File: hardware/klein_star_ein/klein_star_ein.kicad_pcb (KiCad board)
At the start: 6 copper layers, 100 x 90 mm, 184 parts, among them J1 USB_A, J10 AudioJack3_Ground_Switch, J11 AudioJack3_Ground_Switch, J12 AudioJack3_Ground_Switch, J2 DB15_Female_HighDensity_Mount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, J3 Bus_PCI_Express_x1, J4 1367073-1, J5 RJ45_LED_Shielded, J6 USB_C_Receptacle, J7 MEM2051-00-195-00-A, J8 AudioJack3_Ground_Switch, J9 AudioJack3_Ground_Switch, U1 ECP5UM25, U10 SN74ALVC245PWR, U11 KSZ9021RL, U12 TUSB2036, U13 TPS2041B, U2 MT41K512M16, U3 MT41K512M16, U4 FT2232HQ, U5 W25Q128JVS, U6 USB3300-EZK, U7 USB3300-EZK, U8 SN74ALVC245PWR, U9 SN74ALVC245PWR

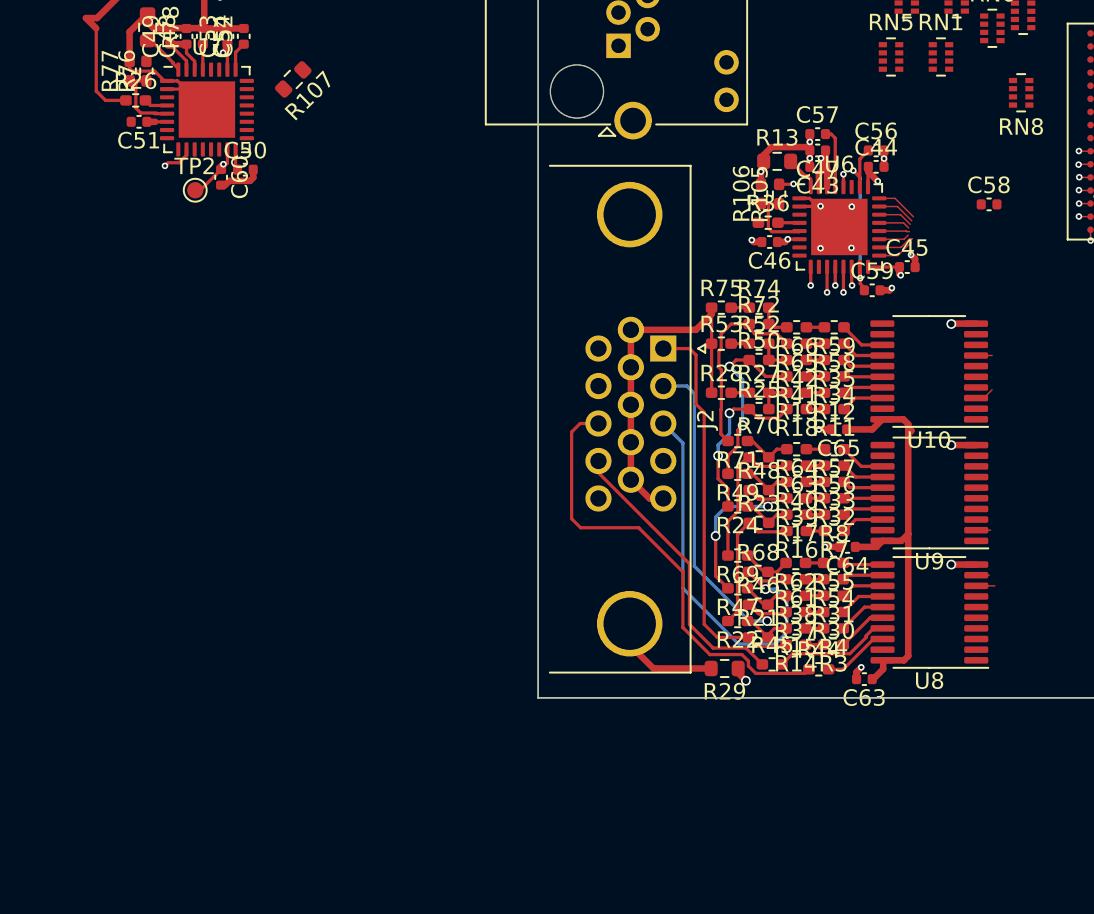
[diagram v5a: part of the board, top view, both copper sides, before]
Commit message: changed VGA drivers to use resistor networks
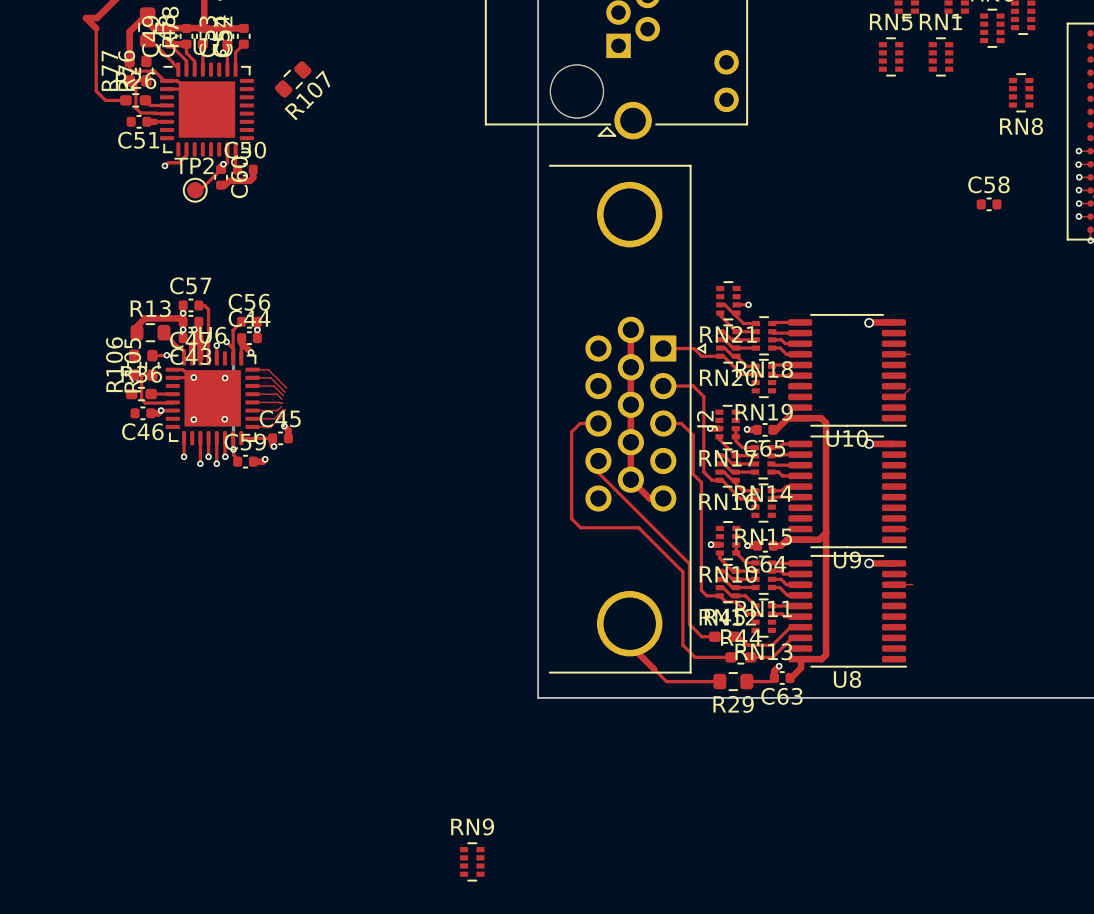
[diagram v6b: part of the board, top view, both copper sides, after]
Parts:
- removed R11, R12, R14, R15, R16, R17, R18, R19, R21, R22, R23, R24, R25, R27, R28, R3, R30, R31, R32, R33, R34, R35, R37, R38, R39, R4, R40, R41, R42, R46, R47, R48, R49, R50, R52, R53, R54, R55, R56, R57, R58, R59, R61, R62, R63, R64, R65, R66, R68, R69, R7, R70, R71, R72, R74, R75, R8: R, Resistor_SMD:R_0402_1005Metric_Pad0.72x0.64mm_HandSolder
- added RN10: 51R, Resistor_SMD:R_Array_Concave_4x0402, F.Cu at (109.6, 140.4)
- added RN11: 51R, Resistor_SMD:R_Array_Concave_4x0402, F.Cu at (111.8, 142.5)
- added RN12: 51R, Resistor_SMD:R_Array_Concave_4x0402, F.Cu at (109.6, 143.0)
- added RN13: 51R, Resistor_SMD:R_Array_Concave_4x0402, F.Cu at (111.8, 145.1)
- added RN14: 51R, Resistor_SMD:R_Array_Concave_4x0402, F.Cu at (111.8, 135.4)
- added RN15: 51R, Resistor_SMD:R_Array_Concave_4x0402, F.Cu at (111.8, 138.1)
- added RN16: 51R, Resistor_SMD:R_Array_Concave_4x0402, F.Cu at (109.6, 135.9)
- added RN17: 51R, Resistor_SMD:R_Array_Concave_4x0402, F.Cu at (109.6, 133.3)
- added RN18: 51R, Resistor_SMD:R_Array_Concave_4x0402, F.Cu at (111.8, 127.9)
- added RN19: 51R, Resistor_SMD:R_Array_Concave_4x0402, F.Cu at (111.8, 130.5)
- added RN20: 51R, Resistor_SMD:R_Array_Concave_4x0402, F.Cu at (109.6, 128.4)
- added RN21: 51R, Resistor_SMD:R_Array_Concave_4x0402, F.Cu at (109.6, 125.7)
- added RN9: 51R, Resistor_SMD:R_Array_Concave_4x0402, F.Cu at (94.0, 160.0)
- moved C46 39.7 mm to (73.9, 132.6)
- moved C47 39.7 mm to (76.8, 127.0)
- moved C56 39.7 mm to (80.4, 127.0)
- moved C57 39.7 mm to (76.8, 126.0)
- moved C59 39.7 mm to (80.1, 135.6)
- moved R105 39.7 mm to (74.4, 129.7)
- moved R106 39.7 mm to (73.3, 129.7)
- moved R13 39.7 mm to (74.3, 127.7)
- moved R36 39.7 mm to (73.8, 131.4)
- moved U6 39.7 mm to (78.1, 131.7)
- moved C43 39.7 mm to (76.8, 128.0)
- moved C44 39.7 mm to (80.4, 128.0)
- moved C45 39.7 mm to (82.3, 134.1)
- moved U10 5.02 mm to (116.9, 130.0)
- moved C64 5.02 mm to (111.9, 140.7)
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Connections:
- U10 pad 11: unconnected-(U10-Pad11) -> /VGA_BUF_B_5
- U10 pad 12: unconnected-(U10-Pad12) -> /VGA_BUF_B_4
- U10 pad 13: /VGA_BUF_B_5 -> /VGA_BUF_B_3
- U10 pad 14: /VGA_BUF_B_4 -> /VGA_BUF_B_2
- U10 pad 15: /VGA_BUF_G_5 -> /VGA_BUF_B_1
- U10 pad 16: /VGA_BUF_G_4 -> /VGA_BUF_B_0
- U10 pad 17: /VGA_BUF_R_5 -> unconnected-(U10-Pad17)
- U10 pad 18: /VGA_BUF_R_4 -> unconnected-(U10-Pad18)
- U8 pad 11: /VGA_BUF_B_1 -> /VGA_BUF_R_5
- U8 pad 12: /VGA_BUF_B_0 -> /VGA_BUF_R_4
- U8 pad 13: /VGA_BUF_G_1 -> /VGA_BUF_R_3
- U8 pad 14: /VGA_BUF_G_0 -> /VGA_BUF_R_2
- U9 pad 11: unconnected-(U9-Pad11) -> /VGA_BUF_G_5
- U9 pad 12: unconnected-(U9-Pad12) -> /VGA_BUF_G_4
- U9 pad 13: /VGA_BUF_B_3 -> /VGA_BUF_G_3
- U9 pad 14: /VGA_BUF_B_2 -> /VGA_BUF_G_2
- U9 pad 15: /VGA_BUF_G_3 -> /VGA_BUF_G_1
- U9 pad 16: /VGA_BUF_G_2 -> /VGA_BUF_G_0
- U9 pad 17: /VGA_BUF_R_3 -> unconnected-(U9-Pad17)
- U9 pad 18: /VGA_BUF_R_2 -> unconnected-(U9-Pad18)
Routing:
- net /VGA_AR: track 24.4 -> 6.30 mm
- net Net-(R65-Pad2): track 12.0 -> 0.00 mm
- net /VGA_AG: track 22.7 -> 11.2 mm, vias 1 -> 0
- net Net-(R41-Pad2): track 11.3 -> 0.00 mm, vias 2 -> 0
- net Net-(R39-Pad2): track 11.3 -> 0.00 mm, vias 2 -> 0
- net GND: track 135.2 -> 124.1 mm
- net Net-(R18-Pad2): track 10.3 -> 0.00 mm, vias 2 -> 0
- net /VGA_AB: track 25.4 -> 15.7 mm, vias 1 -> 0
- net Net-(R63-Pad2): track 9.15 -> 0.00 mm
- net Net-(R16-Pad2): track 9.09 -> 0.00 mm
- net Net-(J2-Pad13): track 27.8 -> 23.0 mm
- net Net-(J2-Pad14): track 17.8 -> 14.2 mm
- net Net-(R17-Pad2): track 3.03 -> 0.00 mm
- net Net-(R64-Pad2): track 3.03 -> 0.00 mm
- net Net-(R40-Pad2): track 3.03 -> 0.00 mm
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
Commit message: a
a
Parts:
- J5: value RJ45_LED_Shielded -> ARJM11C7-502-AB-ER2-T; footprint Connector_RJ:RJ45_Amphenol_RJHSE538X -> footprints:ABRACON_ARJM11C7-502-AB-ER2-T
- moved RN1 66.2 mm to (59.3, 130.2)
- moved RN2 66.2 mm to (57.2, 126.6)
- moved RN6 66.2 mm to (62.5, 128.4)
- moved RN4 66.2 mm to (60.3, 126.6)
- moved RN7 66.2 mm to (64.3, 127.7)
- moved RN8 66.2 mm to (64.2, 132.4)
- moved U5 66.2 mm to (58.0, 119.1)
- moved RN5 66.2 mm to (56.3, 130.2)
- moved C62 59.7 mm to (132.0, 87.6), turned to 0 degrees
- moved R77 58.8 mm to (125.8, 85.7), turned to 0 degrees
- moved R78 58.7 mm to (128.4, 86.8), turned to 180 degrees
- moved C61 58.1 mm to (135.4, 91.0), turned to -90 degrees
- moved R26 57.5 mm to (124.0, 86.1), turned to -90 degrees
- moved R76 57.4 mm to (125.8, 86.7), turned to 0 degrees
- moved C51 56.7 mm to (122.7, 86.3), turned to 90 degrees
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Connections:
- J5 pad 1: unconnected-(J5-Pad1) -> Net-(U11-Pad1)
- J5 pad 10: unconnected-(J5-Pad10) -> Net-(U11-Pad15)
- J5 pad 2: unconnected-(J5-Pad2) -> Net-(U11-Pad2)
- J5 pad 3: unconnected-(J5-Pad3) -> Net-(U11-Pad7)
- J5 pad 4: unconnected-(J5-Pad4) -> Net-(U11-Pad8)
- J5 pad 7: unconnected-(J5-Pad7) -> Net-(U11-Pad10)
- J5 pad 8: unconnected-(J5-Pad8) -> Net-(U11-Pad11)
- J5 pad 9: unconnected-(J5-Pad9) -> Net-(U11-Pad14)
- U11 pad 1: unconnected-(U11-Pad1) -> Net-(U11-Pad1)
- U11 pad 10: unconnected-(U11-Pad10) -> Net-(U11-Pad10)
- U11 pad 11: unconnected-(U11-Pad11) -> Net-(U11-Pad11)
- U11 pad 14: unconnected-(U11-Pad14) -> Net-(U11-Pad14)
- U11 pad 15: unconnected-(U11-Pad15) -> Net-(U11-Pad15)
- U11 pad 2: unconnected-(U11-Pad2) -> Net-(U11-Pad2)
- U11 pad 7: unconnected-(U11-Pad7) -> Net-(U11-Pad7)
- U11 pad 8: unconnected-(U11-Pad8) -> Net-(U11-Pad8)
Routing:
- net GND: track 124.1 -> 102.1 mm, vias 41 -> 21
- net /DRAM_DATA_20: track 21.4 -> 0.00 mm, vias 2 -> 0
- net /DRAM_DATA_8: track 19.9 -> 0.00 mm, vias 2 -> 0
- net /DRAM_DATA_10: track 19.8 -> 0.00 mm, vias 2 -> 0
- net /DRAM_DM2: track 19.8 -> 0.00 mm, vias 2 -> 0
- net /DRAM_DATA_5: track 19.8 -> 0.00 mm, vias 2 -> 0
- net /DRAM_DQS2_P: track 19.8 -> 0.00 mm, vias 2 -> 0
- net /DRAM_DATA_14: track 19.8 -> 0.00 mm, vias 2 -> 0
- net /DRAM_DQS2_N: track 19.8 -> 0.00 mm, vias 2 -> 0
- net /DRAM_DQS1_N: track 19.8 -> 0.00 mm, vias 2 -> 0
- net /DRAM_DM3: track 19.8 -> 0.00 mm, vias 2 -> 0
- net /DRAM_DQS0_N: track 19.8 -> 0.00 mm, vias 2 -> 0
- net /DRAM_DQS1_P: track 19.8 -> 0.00 mm, vias 2 -> 0
- net /DRAM_DATA_29: track 19.8 -> 0.00 mm, vias 2 -> 0
- net /DRAM_DATA_27: track 19.8 -> 0.00 mm, vias 2 -> 0
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
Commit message: dram layout
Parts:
- removed R1, R6: 0R, Resistor_SMD:R_0603_1608Metric
- removed RN8: 51R, Resistor_SMD:R_Array_Concave_4x0402
- added C66: 470n, Capacitor_SMD:C_0402_1005Metric, F.Cu at (170.2, 124.7)
- C11, C13, C39, C40, C41, C42, C55, C8, R79, R80: moved to B.Cu
- moved C2 116.4 mm to (158.9, 121.2), turned to 180 degrees
- moved C7 113.8 mm to (159.2, 130.1), turned to 90 degrees
- moved C36 111.0 mm to (161.9, 132.9), turned to 180 degrees
- moved RN5 110.1 mm to (164.8, 148.8), turned to 90 degrees
- moved RN6 109.7 mm to (170.7, 146.4)
- moved RN7 107.6 mm to (170.7, 143.7)
- moved RN2 103.1 mm to (158.8, 144.2)
- moved C3 102.2 mm to (170.6, 129.2), turned to 90 degrees
- moved RN4 100.6 mm to (158.8, 146.8)
- moved RN1 100.1 mm to (158.8, 141.6)
- moved C8 98.5 mm to (160.2, 146.3), turned to -90 degrees
- moved C9 93.8 mm to (159.2, 125.1), turned to 90 degrees
- moved C37 90.8 mm to (167.5, 133.3)
- moved C35 90.1 mm to (159.2, 136.8), turned to -90 degrees
- moved C17 90.1 mm to (159.2, 134.7), turned to -90 degrees
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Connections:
- C1 pad 1: /DRAM_1_VCORE -> 1V35_DRAM_VCORE
- C10 pad 1: /DRAM_2_VCORE -> 1V35_DRAM_VCORE
- C12 pad 1: /DRAM_1_VCORE -> 1V35_DRAM_VCORE
- C13 pad 1: /DRAM_2_VCORE -> 1V35_DRAM_VCORE
- C14 pad 1: /DRAM_2_VCORE -> 1V35_DRAM_VCORE
- C15 pad 1: /DRAM_1_VCORE -> 1V35_DRAM_VCORE
- C16 pad 1: /DRAM_2_VCORE -> 1V35_DRAM_VCORE
- C17 pad 1: /DRAM_2_VCORE -> 1V35_DRAM_VCORE
- C18 pad 1: /DRAM_1_VCORE -> 1V35_DRAM_VCORE
- C19 pad 1: /DRAM_2_VCORE -> 1V35_DRAM_VCORE
- C2 pad 1: /DRAM_1_VCORE -> 1V35_DRAM_VCORE
- C20 pad 1: /DRAM_1_VCORE -> 1V35_DRAM_VCORE
- C3 pad 1: /DRAM_1_VCORE -> 1V35_DRAM_VCORE
- C35 pad 1: /DRAM_2_VCORE -> 1V35_DRAM_VCORE
- C36 pad 1: /DRAM_1_VCORE -> 1V35_DRAM_VCORE
- C37 pad 1: /DRAM_2_VCORE -> 1V35_DRAM_VCORE
- C38 pad 1: /DRAM_1_VCORE -> 1V35_DRAM_VCORE
- C39 pad 1: /DRAM_2_VCORE -> 1V35_DRAM_VCORE
- C4 pad 1: /DRAM_2_VCORE -> 1V35_DRAM_VCORE
- C5 pad 1: /DRAM_1_VCORE -> 1V35_DRAM_VCORE
- C6 pad 1: /DRAM_2_VCORE -> 1V35_DRAM_VCORE
- C7 pad 1: /DRAM_1_VCORE -> 1V35_DRAM_VCORE
- C8 pad 1: /DRAM_2_VCORE -> 1V35_DRAM_VCORE
- C9 pad 1: /DRAM_1_VCORE -> 1V35_DRAM_VCORE
- RN1 pad 1: /DRAM_ADDR_13 -> GND
- RN1 pad 2: /DRAM_ADDR_7 -> GND
- RN1 pad 3: /DRAM_ADDR_9 -> GND
- RN1 pad 4: /DRAM_ADDR_5 -> GND
- RN1 pad 5: GND -> /DRAM_nCS
- RN1 pad 6: GND -> /DRAM_ODT
- RN1 pad 7: GND -> /DRAM_nCAS
- RN1 pad 8: GND -> /DRAM_nRAS
- RN2 pad 1: /DRAM_ADDR_2 -> GND
- RN2 pad 2: /DRAM_ADDR_3 -> GND
- RN2 pad 3: /DRAM_ADDR_0 -> GND
- RN2 pad 4: /DRAM_ADDR_BA2 -> GND
- RN2 pad 5: GND -> /DRAM_ADDR_3
- RN2 pad 6: GND -> /DRAM_ADDR_0
- RN2 pad 7: GND -> /DRAM_ADDR_BA2
- RN2 pad 8: GND -> /DRAM_ADDR_BA0
- RN4 pad 1: /DRAM_ADDR_BA0 -> GND
- RN4 pad 2: /DRAM_nCS -> GND
- RN4 pad 3: /DRAM_nWE -> GND
- RN4 pad 4: /DRAM_ODT -> unconnected-(RN4-Pad4)
- RN4 pad 5: GND -> unconnected-(RN4-Pad5)
- RN4 pad 6: GND -> /DRAM_ADDR_7
- RN4 pad 7: GND -> /DRAM_ADDR_2
- RN4 pad 8: GND -> /DRAM_ADDR_5
- RN5 pad 1: /DRAM_nCAS -> GND
- RN5 pad 2: /DRAM_nRAS -> GND
- RN5 pad 3: unconnected-(RN5-Pad3) -> GND
- RN5 pad 4: unconnected-(RN5-Pad4) -> GND
- RN5 pad 5: unconnected-(RN5-Pad5) -> /DRAM_ADDR_14
- RN5 pad 6: unconnected-(RN5-Pad6) -> /DRAM_ADDR_11
- RN5 pad 7: GND -> /DRAM_ADDR_9
- RN5 pad 8: GND -> /DRAM_ADDR_13
- RN6 pad 1: /DRAM_ADDR_11 -> /DRAM_ADDR_BA1
- RN6 pad 2: /DRAM_ADDR_6 -> /DRAM_ADDR_4
- RN6 pad 3: /DRAM_ADDR_8 -> /DRAM_ADDR_6
- RN6 pad 4: /DRAM_ADDR_14 -> /DRAM_ADDR_8
- RN7 pad 1: /DRAM_ADDR_BA1 -> /DRAM_ADDR_10
- RN7 pad 2: /DRAM_ADDR_12 -> /DRAM_ADDR_15
- RN7 pad 3: /DRAM_ADDR_1 -> /DRAM_ADDR_12
- RN7 pad 4: /DRAM_ADDR_4 -> /DRAM_ADDR_1
- U1 pad A12: Net-(U1-PadA13) -> /DRAM_nWE
- U1 pad A13: Net-(U1-PadA13) -> /DRAM_ADDR_BA1
- U1 pad A14: Net-(U1-PadA13) -> /DRAM_ADDR_4
- U1 pad A16: Net-(U1-PadA13) -> /DRAM_ADDR_14
- U1 pad A17: Net-(U1-PadA13) -> /DRAM_nRAS
- U1 pad A18: Net-(U1-PadA13) -> /DRAM_ADDR_BA0
- U1 pad A19: Net-(U1-PadA13) -> /DRAM_nCAS
- U1 pad B12: Net-(U1-PadA13) -> /DRAM_ADDR_15
- U1 pad B13: Net-(U1-PadA13) -> /DRAM_ADDR_1
- U1 pad B15: Net-(U1-PadA13) -> /DRAM_ADDR_6
- U1 pad B16: Net-(U1-PadA13) -> unconnected-(U1-PadB16)
- U1 pad B17: Net-(U1-PadA13) -> unconnected-(U1-PadB17)
- U1 pad B18: Net-(U1-PadA13) -> unconnected-(U1-PadB18)
- U1 pad B19: Net-(U1-PadA13) -> /DRAM_nCS
- U1 pad B20: Net-(U1-PadA13) -> /DRAM_ADDR_12
- U1 pad B3: /DRAM_DATA_6 -> unconnected-(U1-PadB3)
- U1 pad B4: /DRAM_DATA_4 -> unconnected-(U1-PadB4)
- U1 pad C12: Net-(U1-PadA13) -> /DRAM_ADDR_10
- U1 pad C13: Net-(U1-PadA13) -> unconnected-(U1-PadC13)
- U1 pad C14: Net-(U1-PadA13) -> /DRAM_ADDR_11
- U1 pad C15: Net-(U1-PadA13) -> /DRAM_ADDR_5
- U1 pad C16: Net-(U1-PadA13) -> /DRAM_ADDR_8
- U1 pad C17: Net-(U1-PadA13) -> /DRAM_ADDR_0
- U1 pad C18: /DRAM_DM2 -> /DRAM_DATA_4
- U1 pad C4: /DRAM_DATA_5 -> unconnected-(U1-PadC4)
- U1 pad C5: /DRAM_DATA_7 -> unconnected-(U1-PadC5)
- U1 pad D11: Net-(U1-PadA13) -> /DRAM_CKE
- U1 pad D12: Net-(U1-PadA13) -> /DRAM_CLK_P
- U1 pad D13: Net-(U1-PadA13) -> /DRAM_ADDR_3
- U1 pad D14: Net-(U1-PadA13) -> /DRAM_nRESET
- U1 pad D15: Net-(U1-PadA13) -> /DRAM_ADDR_2
- U1 pad D16: Net-(U1-PadA13) -> /DRAM_ADDR_BA2
- U1 pad D17: /DRAM_DATA_19 -> /DRAM_DATA_6
- U1 pad D18: /DRAM_DATA_17 -> /DRAM_DATA_7
- U1 pad D19: /DRAM_DATA_30 -> unconnected-(U1-PadD19)
- U1 pad D20: unconnected-(U1-PadD20) -> DRAM_VREF
- U1 pad D5: /DRAM_DQS0_N -> unconnected-(U1-PadD5)
- U1 pad E1: /DRAM_DATA_11 -> unconnected-(U1-PadE1)
- U1 pad E11: Net-(U1-PadA13) -> unconnected-(U1-PadE11)
- U1 pad E12: Net-(U1-PadA13) -> /DRAM_CLK_N
- U1 pad E13: Net-(U1-PadA13) -> /DRAM_ADDR_13
- U1 pad E14: Net-(U1-PadA13) -> /DRAM_ADDR_7
- U1 pad E15: Net-(U1-PadA13) -> /DRAM_ADDR_9
- U1 pad E16: /DRAM_DATA_21 -> unconnected-(U1-PadE16)
- U1 pad E17: /DRAM_DATA_22 -> unconnected-(U1-PadE17)
- U1 pad E18: /DRAM_DATA_23 -> /DRAM_DATA_5
- U1 pad E19: /DRAM_DATA_28 -> /DRAM_DM1
- U1 pad E2: /DRAM_DATA_13 -> unconnected-(U1-PadE2)
- U1 pad E4: /DRAM_DQS0_P -> unconnected-(U1-PadE4)
- U1 pad F11: unconnected-(U1-PadF11) -> 1V35_DRAM_VCORE
- U1 pad F12: unconnected-(U1-PadF12) -> 1V35_DRAM_VCORE
- U1 pad F16: /DRAM_DATA_18 -> unconnected-(U1-PadF16)
- U1 pad F17: /DRAM_DQS2_P -> /DRAM_DQS0_P
- U1 pad F18: /DRAM_DATA_16 -> unconnected-(U1-PadF18)
- U1 pad F19: /DRAM_DATA_26 -> /DRAM_DATA_8
- U1 pad F2: /DRAM_DATA_15 -> unconnected-(U1-PadF2)
- U1 pad F20: unconnected-(U1-PadF20) -> /DRAM_DATA_10
- U1 pad F3: /DRAM_DATA_14 -> unconnected-(U1-PadF3)
- U1 pad G16: /DRAM_DATA_20 -> /DRAM_DATA_1
- U1 pad G18: /DRAM_DQS2_N -> /DRAM_DQS0_N
- U1 pad G19: /DRAM_DQS3_P -> /DRAM_DQS1_P
- U1 pad G20: /DRAM_DATA_24 -> unconnected-(U1-PadG20)
- U1 pad G3: /DRAM_DATA_12 -> unconnected-(U1-PadG3)
- U1 pad G5: /DRAM_DQS1_N -> unconnected-(U1-PadG5)
- U1 pad H14: +1V35 -> 1V35_DRAM_VCORE
- U1 pad H15: +1V35 -> 1V35_DRAM_VCORE
- U1 pad H16: unconnected-(U1-PadH16) -> /DRAM_DATA_3
- U1 pad H17: unconnected-(U1-PadH17) -> /DRAM_DM0
- U1 pad H20: /DRAM_DQS3_N -> /DRAM_DQS1_N
- U1 pad H3: /DRAM_DATA_8 -> unconnected-(U1-PadH3)
- U1 pad H4: /DRAM_DQS1_P -> unconnected-(U1-PadH4)
- U1 pad H5: /DRAM_DATA_10 -> unconnected-(U1-PadH5)
- U1 pad J15: +1V35 -> 1V35_DRAM_VCORE
- U1 pad J16: unconnected-(U1-PadJ16) -> /DRAM_DATA_0
- U1 pad J17: unconnected-(U1-PadJ17) -> /DRAM_DATA_2
- U1 pad J18: /DRAM_DM3 -> /DRAM_DATA_13
- U1 pad J19: /DRAM_DATA_31 -> /DRAM_DATA_9
- U1 pad J20: /DRAM_DATA_25 -> /DRAM_DATA_11
- U1 pad K18: unconnected-(U1-PadK18) -> /DRAM_DATA_15
- U1 pad K19: /DRAM_DATA_29 -> /DRAM_DATA_12
- U1 pad K20: /DRAM_DATA_27 -> /DRAM_DATA_14
- U1 pad L14: unconnected-(U1-PadL14) -> 1V35_DRAM_VCORE
- U1 pad L15: unconnected-(U1-PadL15) -> 1V35_DRAM_VCORE
- U1 pad L17: unconnected-(U1-PadL17) -> /DRAM_DATA_25
- U1 pad L18: unconnected-(U1-PadL18) -> /DRAM_DATA_26
- U1 pad M15: unconnected-(U1-PadM15) -> 1V35_DRAM_VCORE
- U1 pad M17: unconnected-(U1-PadM17) -> /DRAM_DQS3_N
- U1 pad M18: unconnected-(U1-PadM18) -> /DRAM_DATA_30
- U1 pad M19: unconnected-(U1-PadM19) -> /DRAM_DATA_29
- U1 pad M20: unconnected-(U1-PadM20) -> /DRAM_DATA_28
- U1 pad N16: unconnected-(U1-PadN16) -> /DRAM_DQS3_P
- U1 pad N18: unconnected-(U1-PadN18) -> /DRAM_DATA_31
- U1 pad P16: unconnected-(U1-PadP16) -> DRAM_VREF
- U1 pad P17: unconnected-(U1-PadP17) -> /DRAM_DATA_27
- U1 pad P19: unconnected-(U1-PadP19) -> /DRAM_DATA_16
- U1 pad P20: unconnected-(U1-PadP20) -> /DRAM_DATA_23
- U1 pad R16: unconnected-(U1-PadR16) -> /DRAM_DATA_24
- U1 pad R17: unconnected-(U1-PadR17) -> /DRAM_DM3
- U1 pad R18: unconnected-(U1-PadR18) -> /DRAM_DQS2_N
- U1 pad T17: unconnected-(U1-PadT17) -> /DRAM_DM2
- U1 pad T19: unconnected-(U1-PadT19) -> /DRAM_DQS2_P
- U1 pad T20: unconnected-(U1-PadT20) -> /DRAM_DATA_20
- U1 pad U16: unconnected-(U1-PadU16) -> /DRAM_DATA_21
- U1 pad U17: unconnected-(U1-PadU17) -> /DRAM_DATA_19
- U1 pad U18: unconnected-(U1-PadU18) -> /DRAM_DATA_17
- U1 pad U19: unconnected-(U1-PadU19) -> /DRAM_DATA_22
- U1 pad U20: unconnected-(U1-PadU20) -> /DRAM_DATA_18
- U2 pad A1: /DRAM_1_VCORE -> 1V35_DRAM_VCORE
- U2 pad A8: /DRAM_1_VCORE -> 1V35_DRAM_VCORE
- U2 pad B2: /DRAM_1_VCORE -> 1V35_DRAM_VCORE
- U2 pad C1: /DRAM_1_VCORE -> 1V35_DRAM_VCORE
- U2 pad C9: /DRAM_1_VCORE -> 1V35_DRAM_VCORE
- U2 pad D2: /DRAM_1_VCORE -> 1V35_DRAM_VCORE
- U2 pad D9: /DRAM_1_VCORE -> 1V35_DRAM_VCORE
- U2 pad E9: /DRAM_1_VCORE -> 1V35_DRAM_VCORE
- U2 pad F1: /DRAM_1_VCORE -> 1V35_DRAM_VCORE
- U2 pad G7: /DRAM_1_VCORE -> 1V35_DRAM_VCORE
- U2 pad H2: /DRAM_1_VCORE -> 1V35_DRAM_VCORE
- U2 pad H9: /DRAM_1_VCORE -> 1V35_DRAM_VCORE
- U2 pad K2: /DRAM_1_VCORE -> 1V35_DRAM_VCORE
- U2 pad K8: /DRAM_1_VCORE -> 1V35_DRAM_VCORE
- U2 pad N1: /DRAM_1_VCORE -> 1V35_DRAM_VCORE
- U2 pad N9: /DRAM_1_VCORE -> 1V35_DRAM_VCORE
- U2 pad R1: /DRAM_1_VCORE -> 1V35_DRAM_VCORE
- U2 pad R9: /DRAM_1_VCORE -> 1V35_DRAM_VCORE
- U3 pad A1: /DRAM_2_VCORE -> 1V35_DRAM_VCORE
- U3 pad A8: /DRAM_2_VCORE -> 1V35_DRAM_VCORE
- U3 pad B2: /DRAM_2_VCORE -> 1V35_DRAM_VCORE
- U3 pad C1: /DRAM_2_VCORE -> 1V35_DRAM_VCORE
- U3 pad C9: /DRAM_2_VCORE -> 1V35_DRAM_VCORE
- U3 pad D2: /DRAM_2_VCORE -> 1V35_DRAM_VCORE
- U3 pad D9: /DRAM_2_VCORE -> 1V35_DRAM_VCORE
- U3 pad E9: /DRAM_2_VCORE -> 1V35_DRAM_VCORE
- U3 pad F1: /DRAM_2_VCORE -> 1V35_DRAM_VCORE
- U3 pad G7: /DRAM_2_VCORE -> 1V35_DRAM_VCORE
- U3 pad H2: /DRAM_2_VCORE -> 1V35_DRAM_VCORE
- U3 pad H9: /DRAM_2_VCORE -> 1V35_DRAM_VCORE
- U3 pad K2: /DRAM_2_VCORE -> 1V35_DRAM_VCORE
- U3 pad K8: /DRAM_2_VCORE -> 1V35_DRAM_VCORE
- U3 pad N1: /DRAM_2_VCORE -> 1V35_DRAM_VCORE
- U3 pad N9: /DRAM_2_VCORE -> 1V35_DRAM_VCORE
- U3 pad R1: /DRAM_2_VCORE -> 1V35_DRAM_VCORE
- U3 pad R9: /DRAM_2_VCORE -> 1V35_DRAM_VCORE
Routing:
- net GND: track 102.1 -> 278.7 mm, vias 21 -> 79
- net 1V35_DRAM_VCORE: track 0.00 -> 104.0 mm, vias 0 -> 44
- net /DRAM_ADDR_10: track 0.00 -> 78.6 mm, vias 0 -> 3
- net /DRAM_ADDR_15: track 0.00 -> 77.6 mm, vias 0 -> 3
- net /DRAM_ADDR_8: track 0.00 -> 76.6 mm, vias 0 -> 3
- net /DRAM_ADDR_BA1: track 0.00 -> 76.6 mm, vias 0 -> 3
- net /DRAM_ADDR_4: track 0.00 -> 76.5 mm, vias 0 -> 3
- net /DRAM_ADDR_2: track 0.00 -> 76.5 mm, vias 0 -> 4
- net /DRAM_ADDR_11: track 0.00 -> 75.9 mm, vias 0 -> 3
- net /DRAM_ADDR_6: track 0.00 -> 75.5 mm, vias 0 -> 3
- net /DRAM_nCS: track 0.00 -> 75.5 mm, vias 0 -> 4
- net /DRAM_ADDR_0: track 0.00 -> 75.1 mm, vias 0 -> 4
- net /DRAM_nCAS: track 0.00 -> 75.0 mm, vias 0 -> 4
- net /DRAM_ADDR_14: track 0.00 -> 74.7 mm, vias 0 -> 3
- net /DRAM_ADDR_BA2: track 0.00 -> 74.7 mm, vias 0 -> 3
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- added copper zone on In3.Cu, net 1V35_DRAM_VCORE
